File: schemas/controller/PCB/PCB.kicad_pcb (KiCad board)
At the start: 2 copper layers, 80 x 75 mm, 10 parts, among them J1 236-102, J2 236-102, J3 236-102, J4 236-102, J5 236-102, J6 236-102, U1 STM32F103C8T6, U2 NRF24L01_Breakout

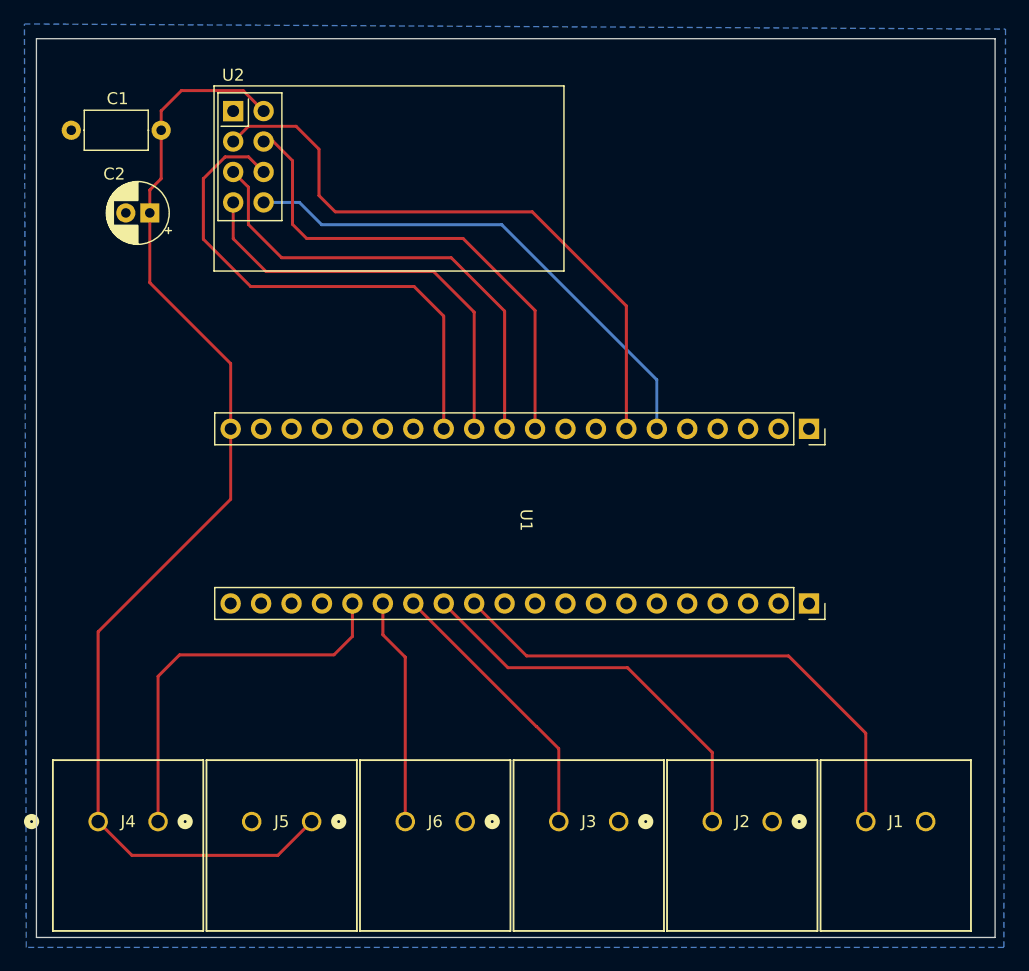
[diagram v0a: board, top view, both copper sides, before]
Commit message: small changes to the PCB layout
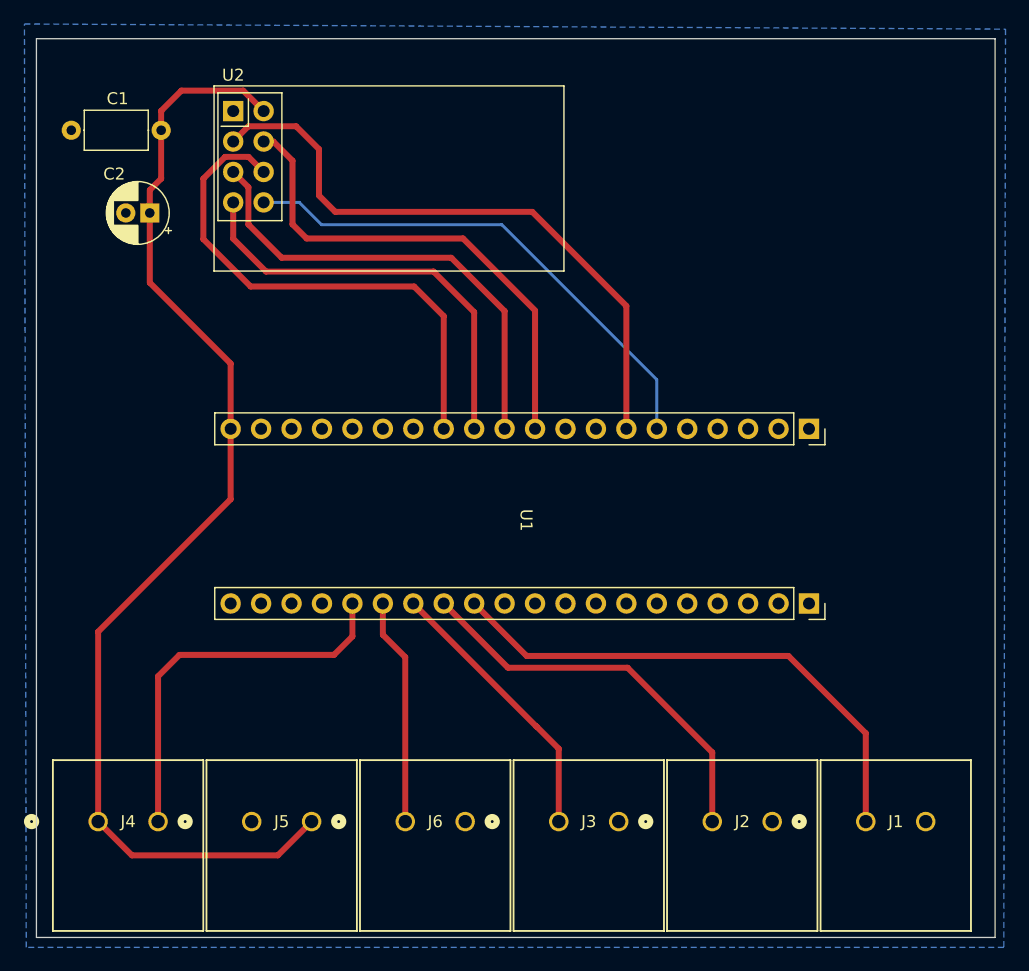
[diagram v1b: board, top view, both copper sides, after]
